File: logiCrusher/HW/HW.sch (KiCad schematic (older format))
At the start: 8 parts, among them J3 Conn_02x05_Odd_Even, U1 R-783.3-0.5

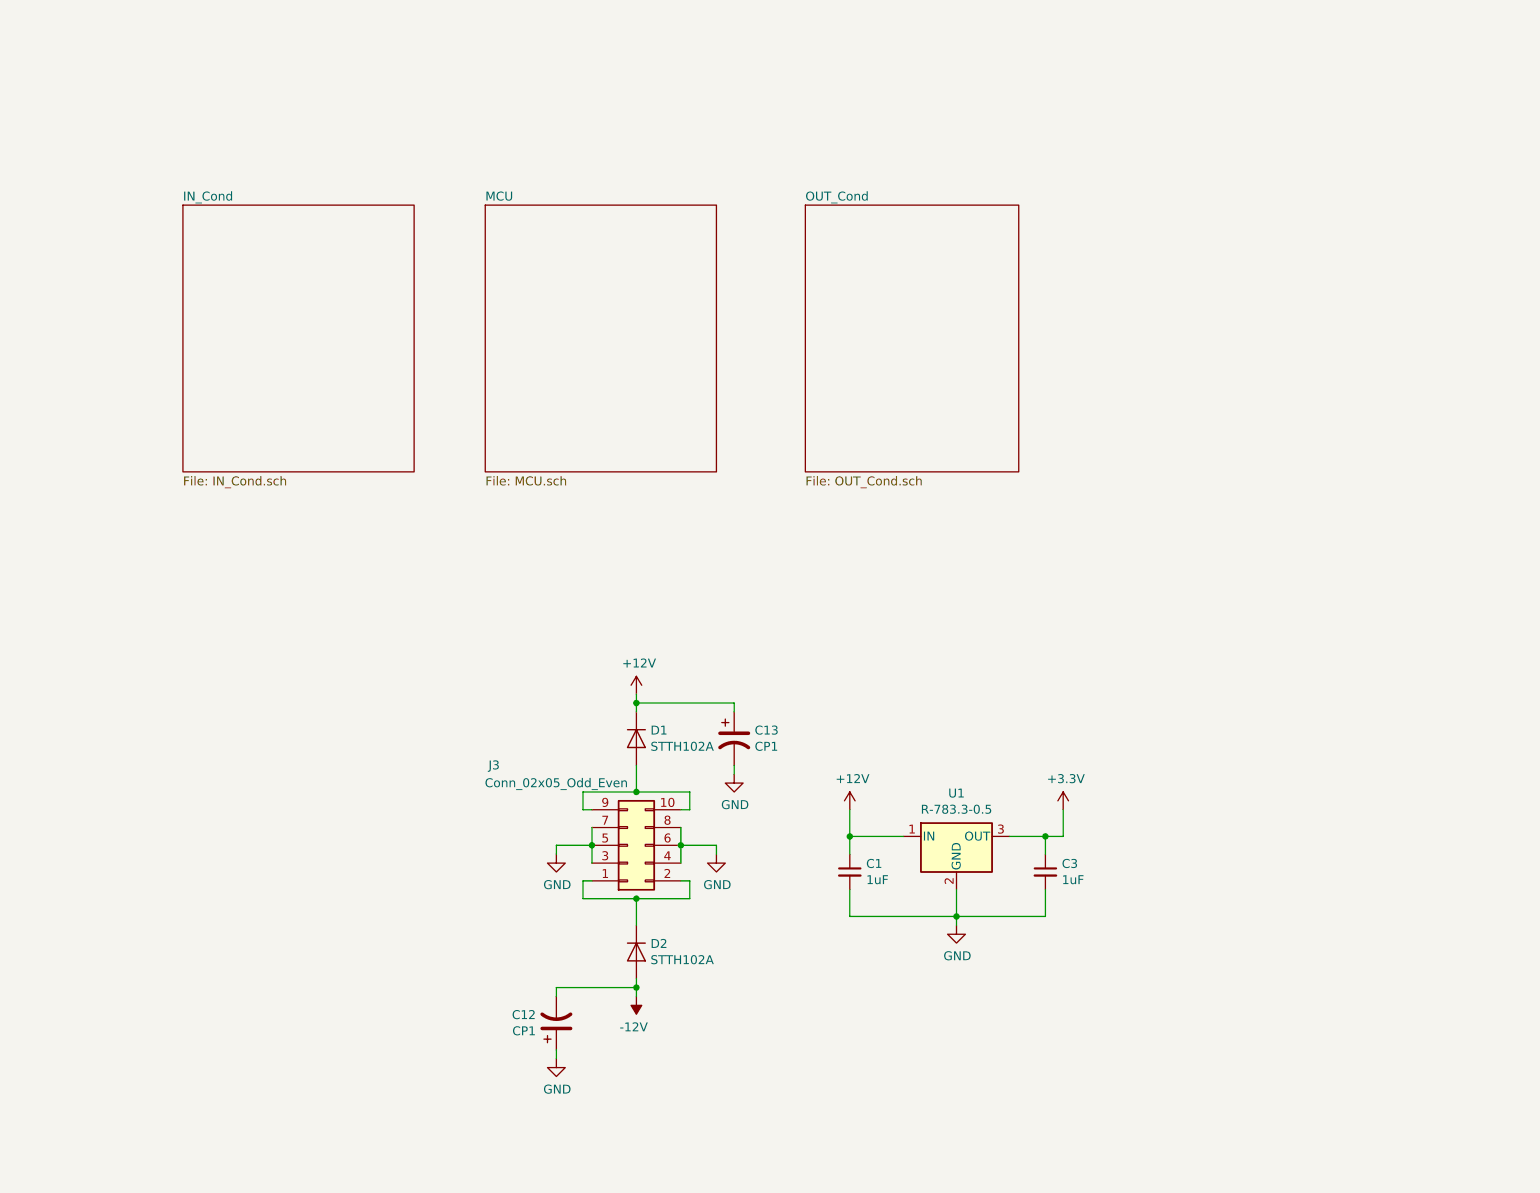
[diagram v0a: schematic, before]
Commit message: Added the front plate files
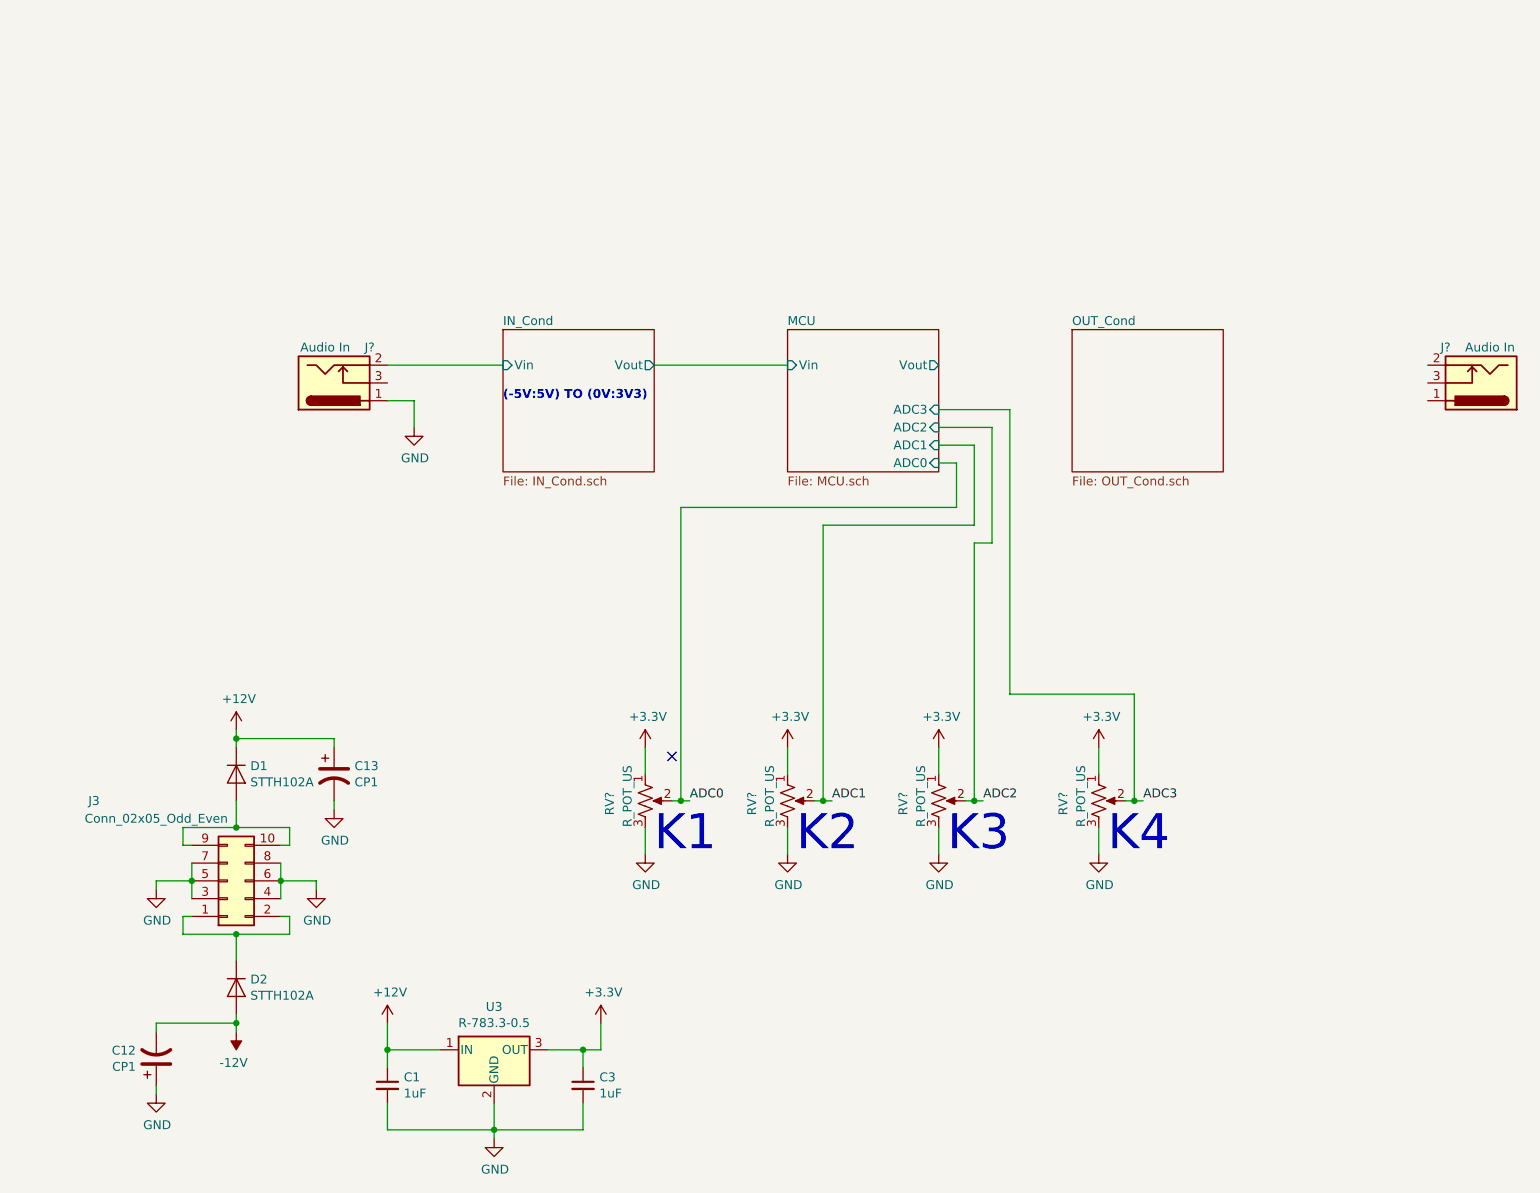
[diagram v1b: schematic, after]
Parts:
- added J? (x2): Audio In, Eurocad:PJ301M-12, symbol Connector:Barrel_Jack_Switch
- added RV? (x4): R_POT_US, symbol Device:R_POT_US
- renumbered U1 to U3
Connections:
- net +3V3: now also RV?.1, RV?.1, RV?.1, RV?.1
- net GND: now also J?.1, RV?.3, RV?.3, RV?.3, RV?.3
- new net ADC0: RV?.2
- new net ADC1: RV?.2
- new net ADC2: RV?.2
- new net ADC3: RV?.2
- new net IN_Cond/Vin: J?.2
- no-connect marks 0 -> 1
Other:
- note added: "(-5V:5V) TO (0V:3V3)"
- note added: "K1"
- note added: "K2"
- note added: "K3"
- note added: "K4"
- moved on the sheet: C1, C12, C13, C3, D1, D2, J3, U3

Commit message: Worked on the HW for the mcu module
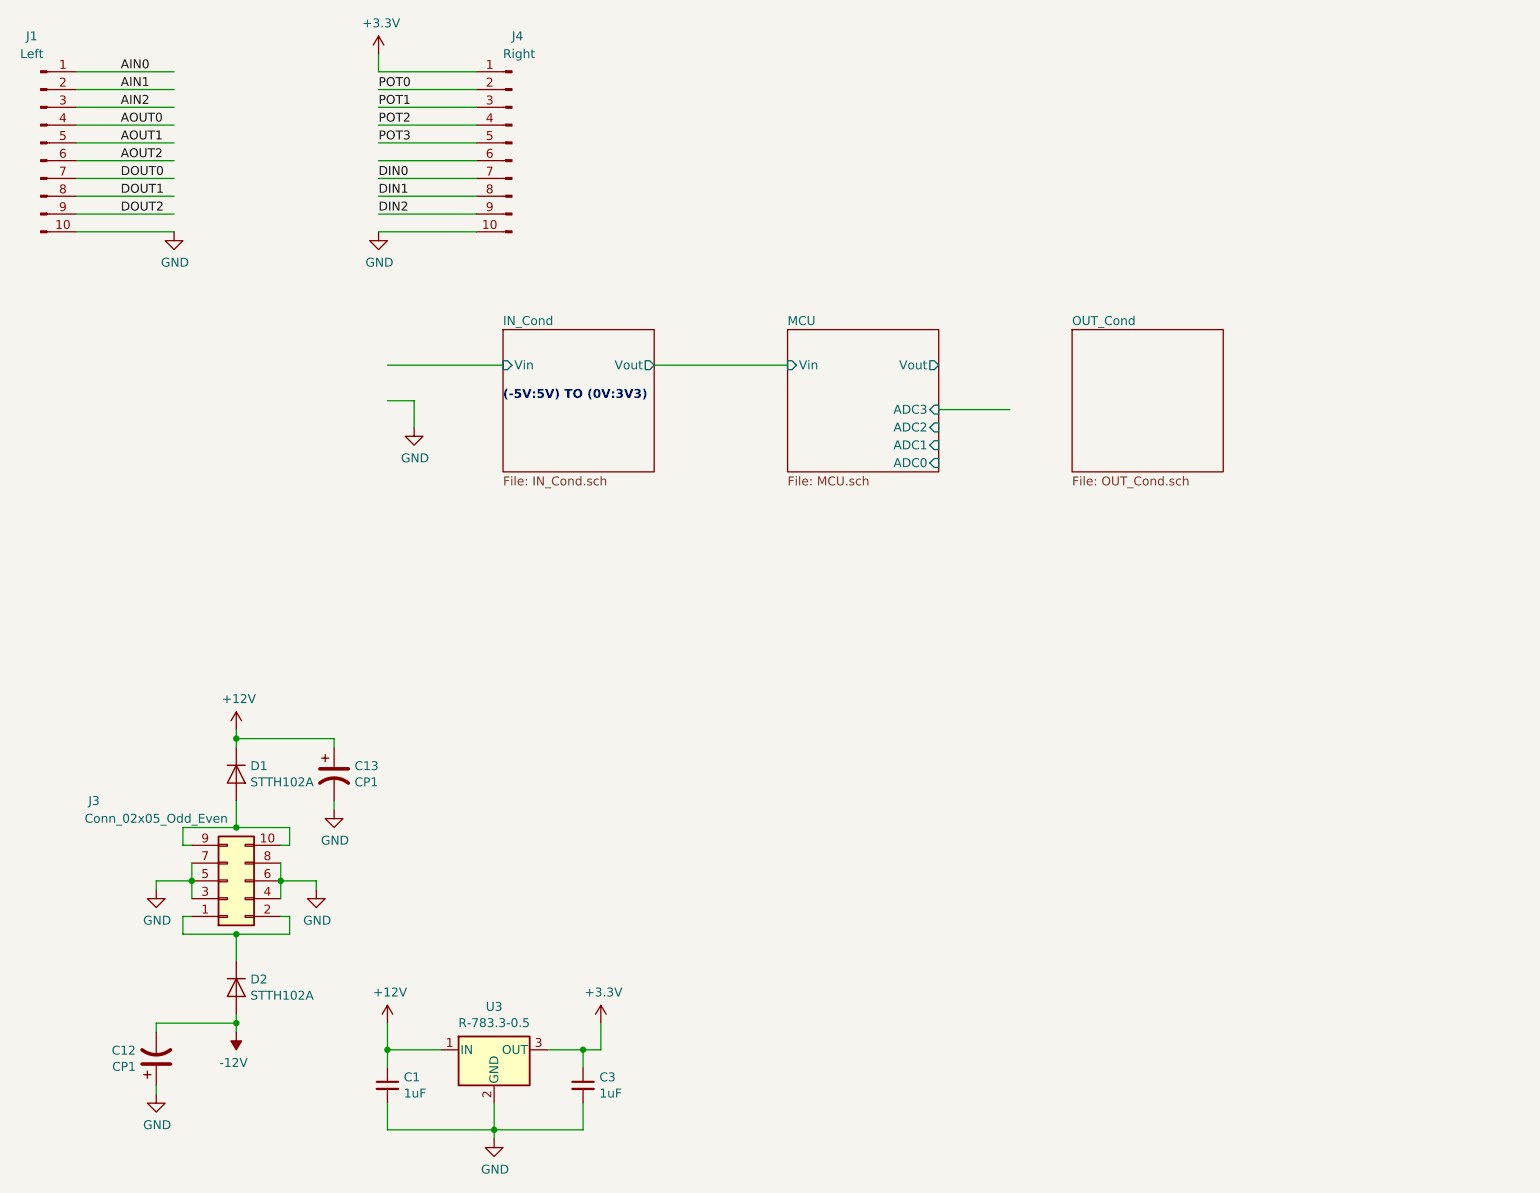
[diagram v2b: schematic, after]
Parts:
- removed J? (x2): Audio In, Eurocad:PJ301M-12, symbol Connector:Barrel_Jack_Switch
- removed RV? (x4): R_POT_US, symbol Device:R_POT_US
- added J1: Left, Connector_PinHeader_2.54mm:PinHeader_1x10_P2.54mm_Vertical, symbol Connector:Conn_01x10_Male
- added J4: Right, Connector_PinHeader_2.54mm:PinHeader_1x10_P2.54mm_Vertical, symbol Connector:Conn_01x10_Male
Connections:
- net labels added: AIN0, AIN1, AIN2, AOUT0, AOUT1, AOUT2, DIN0, DIN1, DIN2, DOUT0, DOUT1, DOUT2, POT0, POT1, POT2, POT3
- net labels removed: ADC0, ADC1, ADC2, ADC3
- wire segments 81 -> 71
- no-connect marks 1 -> 0
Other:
- note removed: "K1"
- note removed: "K2"
- note removed: "K3"
- note removed: "K4"

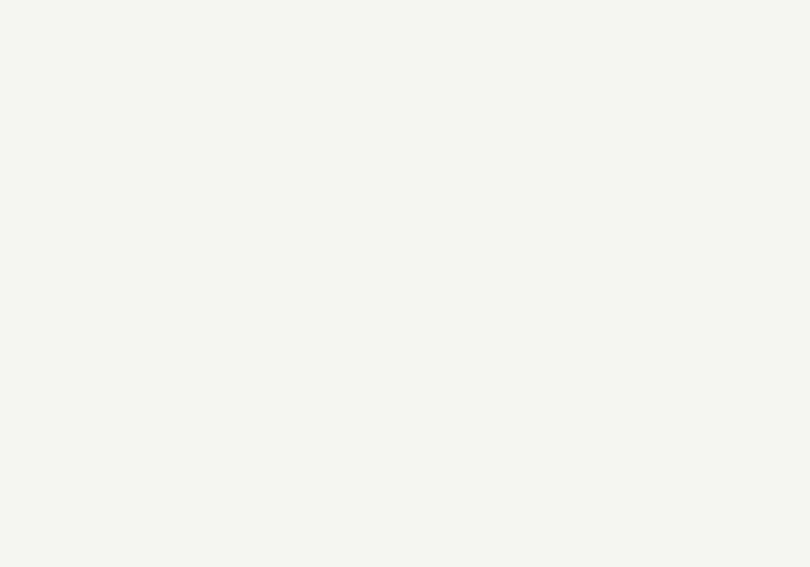
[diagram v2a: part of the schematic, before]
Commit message: Added a switching regulator
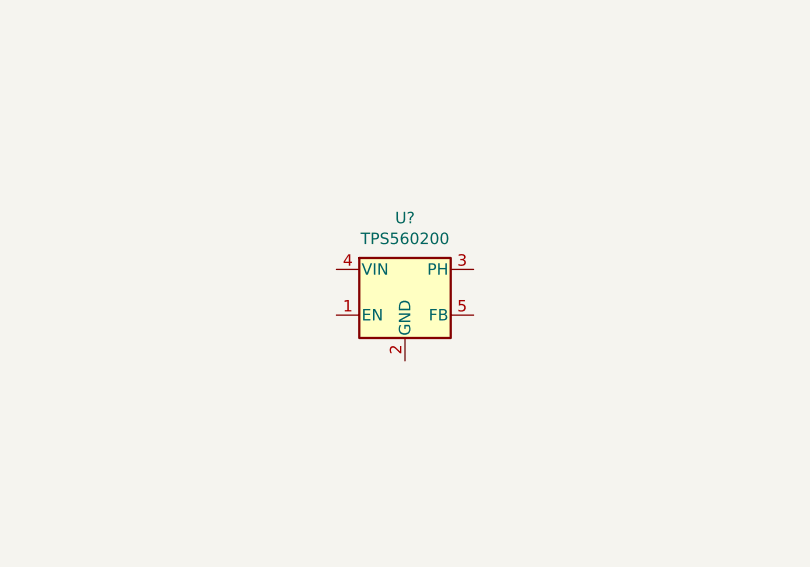
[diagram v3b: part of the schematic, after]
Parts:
- added U?: TPS560200, Package_TO_SOT_SMD:SOT-23-5, symbol Regulator_Switching:TPS560200
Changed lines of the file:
@@
 Text Label 2900 1950 0    50   ~ 0
 DIN2
+$Comp
+L Regulator_Switching:TPS560200 U?
+U 1 1 5CBCC094
+P 4850 4850
+F 0 "U?" H 4850 5175 50  0000 C CNN
+F 1 "TPS560200" H 4850 5084 50  0000 C CNN
+F 2 "Package_TO_SOT_SMD:SOT-23-5" H 4900 4600 50  0001 L CNN
+F 3 "http://www.ti.com/lit/ds/symlink/tps560200.pdf" H 4600 4500 50  0001 C CNN
+	1    4850 4850
+	1    0    0    -1
+$EndComp
 $EndSCHEMATC

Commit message: Added some deps
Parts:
- removed U?: TPS560200, Package_TO_SOT_SMD:SOT-23-5, symbol Regulator_Switching:TPS560200
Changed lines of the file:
@@
 Text Label 2900 1950 0    50   ~ 0
 DIN2
-$Comp
-L Regulator_Switching:TPS560200 U?
-U 1 1 5CBCC094
-P 4850 4850
-F 0 "U?" H 4850 5175 50  0000 C CNN
-F 1 "TPS560200" H 4850 5084 50  0000 C CNN
-F 2 "Package_TO_SOT_SMD:SOT-23-5" H 4900 4600 50  0001 L CNN
-F 3 "http://www.ti.com/lit/ds/symlink/tps560200.pdf" H 4600 4500 50  0001 C CNN
-	1    4850 4850
-	1    0    0    -1
-$EndComp
 $EndSCHEMATC
